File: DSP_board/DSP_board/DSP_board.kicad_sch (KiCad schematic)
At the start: 62 parts

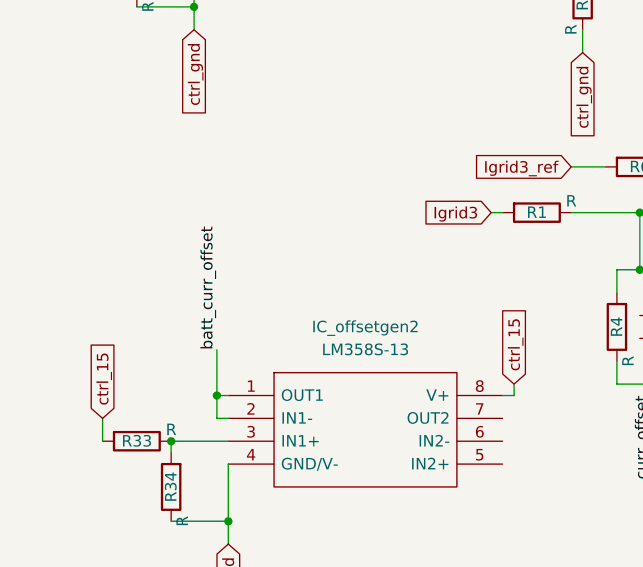
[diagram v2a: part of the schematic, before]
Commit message: adding diodes
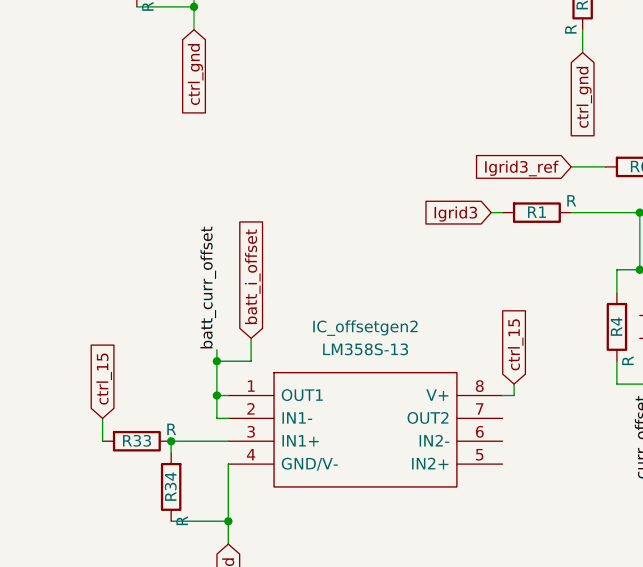
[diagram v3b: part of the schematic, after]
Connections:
- net batt_curr_offset renamed batt_i_offset
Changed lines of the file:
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@@
   (junction (at 100.33 91.44) (diameter 0) (color 0 0 0 0)
   )
+  (junction (at 33.02 120.65) (diameter 0) (color 0 0 0 0)
+  )
   (junction (at 203.2 102.87) (diameter 0) (color 0 0 0 0)
   )
@@
     (stroke (width 0) (type default) (color 0 0 0 0))
   )
-  (wire (pts (xy 33.02 119.38) (xy 33.02 124.46))
+  (wire (pts (xy 33.02 119.38) (xy 33.02 120.65))
     (stroke (width 0) (type default) (color 0 0 0 0))
   )
@@
     (stroke (width 0) (type default) (color 0 0 0 0))
   )
+  (wire (pts (xy 33.02 120.65) (xy 36.83 120.65))
+    (stroke (width 0) (type default) (color 0 0 0 0))
+  )
   (wire (pts (xy 66.04 123.19) (xy 66.04 124.46))
     (stroke (width 0) (type default) (color 0 0 0 0))
@@
     (stroke (width 0) (type default) (color 0 0 0 0))
   )
+  (wire (pts (xy 36.83 118.11) (xy 36.83 120.65))
+    (stroke (width 0) (type default) (color 0 0 0 0))
+  )
   (wire (pts (xy 132.08 161.29) (xy 133.35 161.29))
     (stroke (width 0) (type default) (color 0 0 0 0))
@@
   )
   (wire (pts (xy 95.25 25.4) (xy 95.25 33.02))
+    (stroke (width 0) (type default) (color 0 0 0 0))
+  )
+  (wire (pts (xy 33.02 120.65) (xy 33.02 124.46))
     (stroke (width 0) (type default) (color 0 0 0 0))
   )
@@
     (property "Intersheet References" "${INTERSHEET_REFS}" (id 0) (at 149.9264 87.5506 0)
       (effects (font (size 1.27 1.27)) (justify right) hide)
+    )
+  )
+  (global_label "batt_i_offset" (shape input) (at 36.83 118.11 90) (fields_autoplaced)
+    (effects (font (size 1.27 1.27)) (justify left))
+    (property "Intersheet References" "${INTERSHEET_REFS}" (id 0) (at 36.7506 103.9645 90)
+      (effects (font (size 1.27 1.27)) (justify left) hide)
     )
   )
@@
       (reference "R41") (unit 1) (value "R") (footprint "Resistor_SMD:R_1206_3216Metric_Pad1.30x1.75mm_HandSolder")
     )
-  )
+    (path "/65abaeeb-f079-4d1a-9aaf-277d58cadcf0/633851ea-fd57-461d-8ac8-529a3666fe4d"
+      (reference "R42") (unit 1) (value "R") (footprint "Capacitor_SMD:C_1206_3216Metric_Pad1.33x1.80mm_HandSolder")
+    )
+    (path "/65abaeeb-f079-4d1a-9aaf-277d58cadcf0/03bdad3c-ffe6-4cdd-81ae-8040d9d8d155"
+      (reference "R43") (unit 1) (value "R") (footprint "Capacitor_SMD:C_1206_3216Metric_Pad1.33x1.80mm_HandSolder")
+    )
+    (path "/65abaeeb-f079-4d1a-9aaf-277d58cadcf0/f277b0a6-516a-4ff0-a8ff-91d22b3e0f24"
+      (reference "R44") (unit 1) (value "R") (footprint "Capacitor_SMD:C_1206_3216Metric_Pad1.33x1.80mm_HandSolder")
+    )
+    (path "/65abaeeb-f079-4d1a-9aaf-277d58cadcf0/0721069a-c0ae-471f-acc9-315482680f3f"
+      (reference "R45") (unit 1) (value "R") (footprint "Capacitor_SMD:C_1206_3216Metric_Pad1.33x1.80mm_HandSolder")
+    )
+    (path "/65abaeeb-f079-4d1a-9aaf-277d58cadcf0/9ab50948-5ad5-40a2-89b6-c072b55325a9"
+      (reference "R46") (unit 1) (value "R") (footprint "Capacitor_SMD:C_1206_3216Metric_Pad1.33x1.80mm_HandSolder")
+    )
+    (path "/65abaeeb-f079-4d1a-9aaf-277d58cadcf0/cfd8a5ce-12a8-4557-beb0-11f6d49ec5f5"
+      (reference "R47") (unit 1) (value "R") (footprint "Capacitor_SMD:C_1206_3216Metric_Pad1.33x1.80mm_HandSolder")
+    )
+    (path "/65abaeeb-f079-4d1a-9aaf-277d58cadcf0/0c842a64-1e77-4b78-95e8-7ba90a7cd400"
+      (reference "R48") (unit 1) (value "R") (footprint "Capacitor_SMD:C_1206_3216Metric_Pad1.33x1.80mm_HandSolder")
+    )
+    (path "/65abaeeb-f079-4d1a-9aaf-277d58cadcf0/5d7ea75c-9a45-471b-80b3-8055c1bd3392"
+      (reference "R49") (unit 1) (value "R") (footprint "Capacitor_SMD:C_1206_3216Metric_Pad1.33x1.80mm_HandSolder")
+    )
+    (path "/65abaeeb-f079-4d1a-9aaf-277d58cadcf0/464cc93e-0fa0-422f-a95e-524969a7eda0"
+      (reference "R50") (unit 1) (value "R") (footprint "Capacitor_SMD:C_1206_3216Metric_Pad1.33x1.80mm_HandSolder")
+    )
+    (path "/65abaeeb-f079-4d1a-9aaf-277d58cadcf0/36f6eed7-c17f-41d3-b395-39d6e394c6b2"
+      (reference "R51") (unit 1) (value "R") (footprint "Capacitor_SMD:C_1206_3216Metric_Pad1.33x1.80mm_HandSolder")
+    )
+    (path "/65abaeeb-f079-4d1a-9aaf-277d58cadcf0/18122b88-ddaa-410f-b2f2-d8795197d742"
+      (reference "R52") (unit 1) (value "R") (footprint "Capacitor_SMD:C_1206_3216Metric_Pad1.33x1.80mm_HandSolder")
+    )
+    (path "/65abaeeb-f079-4d1a-9aaf-277d58cadcf0/625ca805-1ca6-46b3-9a7f-e433edb0bf42"
+      (reference "R53") (unit 1) (value "R") (footprint "Capacitor_SMD:C_1206_3216Metric_Pad1.33x1.80mm_HandSolder")
+    )
+    (path "/65abaeeb-f079-4d1a-9aaf-277d58cadcf0/5b55d93e-5df4-46a4-aa3c-60d388486393"
+      (reference "R54") (unit 1) (value "R") (footprint "Capacitor_SMD:C_1206_3216Metric_Pad1.33x1.80mm_HandSolder")
+    )
+    (path "/65abaeeb-f079-4d1a-9aaf-277d58cadcf0/1a7fbe84-d9ba-4889-9d7b-b0ae3680a7af"
+      (reference "R55") (unit 1) (value "R") (footprint "Capacitor_SMD:C_1206_3216Metric_Pad1.33x1.80mm_HandSolder")
+    )
+    (path "/65abaeeb-f079-4d1a-9aaf-277d58cadcf0/73996276-51f1-47c4-ae27-a175edb9c7e6"
+      (reference "R56") (unit 1) (value "R") (footprint "Capacitor_SMD:C_1206_3216Metric_Pad1.33x1.80mm_HandSolder")
+    )
+    (path "/65abaeeb-f079-4d1a-9aaf-277d58cadcf0/5715a765-228c-4f16-a668-cbf136d91dee"
+      (reference "R57") (unit 1) (value "R") (footprint "Capacitor_SMD:C_1206_3216Metric_Pad1.33x1.80mm_HandSolder")
+    )
+    (path "/65abaeeb-f079-4d1a-9aaf-277d58cadcf0/267a327e-b52e-44fc-b43e-e5566558491b"
+      (reference "R58") (unit 1) (value "R") (footprint "Capacitor_SMD:C_1206_3216Metric_Pad1.33x1.80mm_HandSolder")
+    )
+    (path "/65abaeeb-f079-4d1a-9aaf-277d58cadcf0/7c30b4f4-7b3c-4715-b109-400e7966150e"
+      (reference "R59") (unit 1) (value "R") (footprint "Capacitor_SMD:C_1206_3216Metric_Pad1.33x1.80mm_HandSolder")
+    )
+    (path "/65abaeeb-f079-4d1a-9aaf-277d58cadcf0/c539e4bd-2b7e-455f-a234-b5daf351c2ec"
+      (reference "R60") (unit 1) (value "R") (footprint "Capacitor_SMD:C_1206_3216Metric_Pad1.33x1.80mm_HandSolder")
+    )
+    (path "/65abaeeb-f079-4d1a-9aaf-277d58cadcf0/9714e31c-d27f-46f1-ae82-bc567e178fb4"
+      (reference "R61") (unit 1) (value "R") (footprint "Capacitor_SMD:C_1206_3216Metric_Pad1.33x1.80mm_HandSolder")
+    )
+    (path "/65abaeeb-f079-4d1a-9aaf-277d58cadcf0/4e337cbc-4efb-492e-a947-6b9b8e9aac28"
+      (reference "R62") (unit 1) (value "R") (footprint "Capacitor_SMD:C_1206_3216Metric_Pad1.33x1.80mm_HandSolder")
+    )
+    (path "/65abaeeb-f079-4d1a-9aaf-277d58cadcf0/63bbbbc2-e6c2-44cb-b5b6-6066a9f29c1b"
+      (reference "R63") (unit 1) (value "R") (footprint "Capacitor_SMD:C_1206_3216Metric_Pad1.33x1.80mm_HandSolder")
+    )
+    (path "/65abaeeb-f079-4d1a-9aaf-277d58cadcf0/ab46fdd0-9150-4873-843d-5d370692deab"
+      (reference "R64") (unit 1) (value "R") (footprint "Capacitor_SMD:C_1206_3216Metric_Pad1.33x1.80mm_HandSolder")
+    )
+  )
